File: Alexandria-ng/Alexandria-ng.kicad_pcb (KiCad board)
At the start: 4 copper layers, 87 parts, among them J1 Eth0, J10 PoE3, J11 PoE4, J12 FFC, J13 +3.3V, J14 I²C, J2 Eth1, J3 Eth2, J4 Eth3, J5 Eth4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

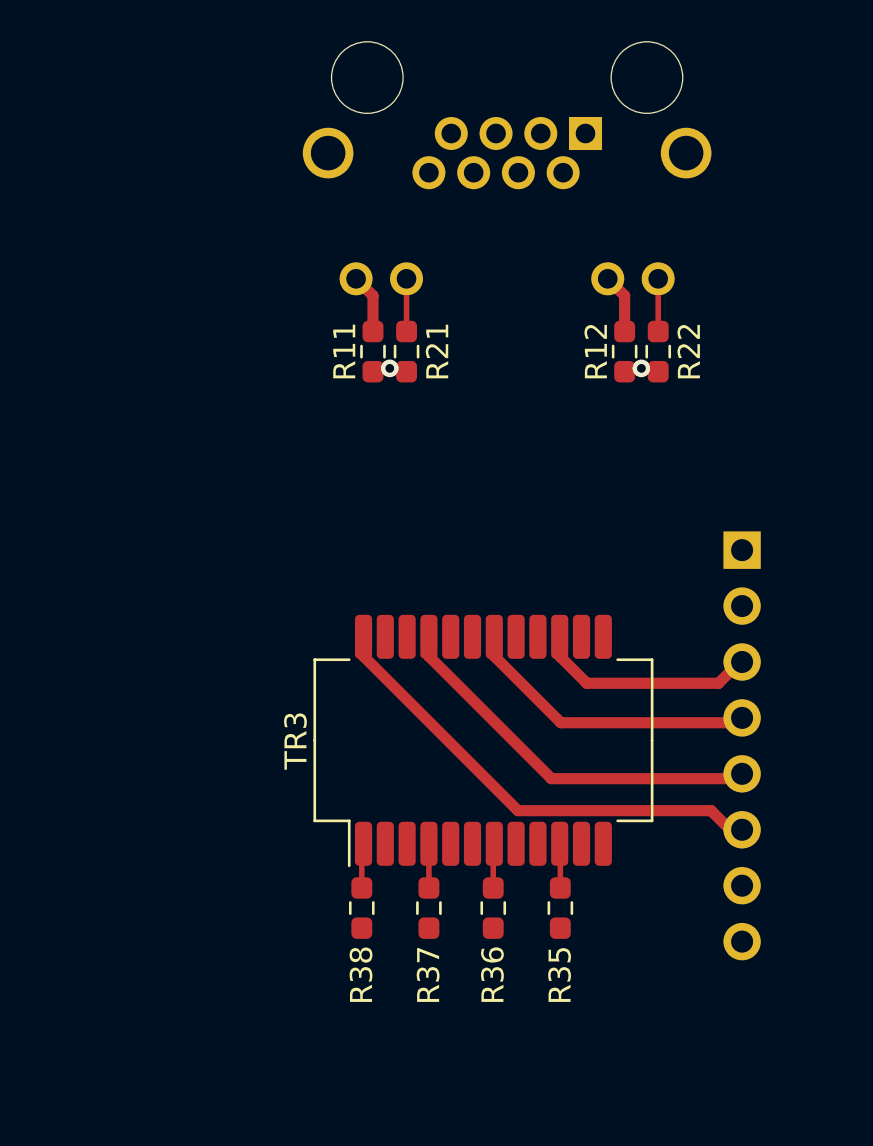
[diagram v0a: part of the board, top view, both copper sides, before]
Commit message: Re-doing Ethernet magnetics area
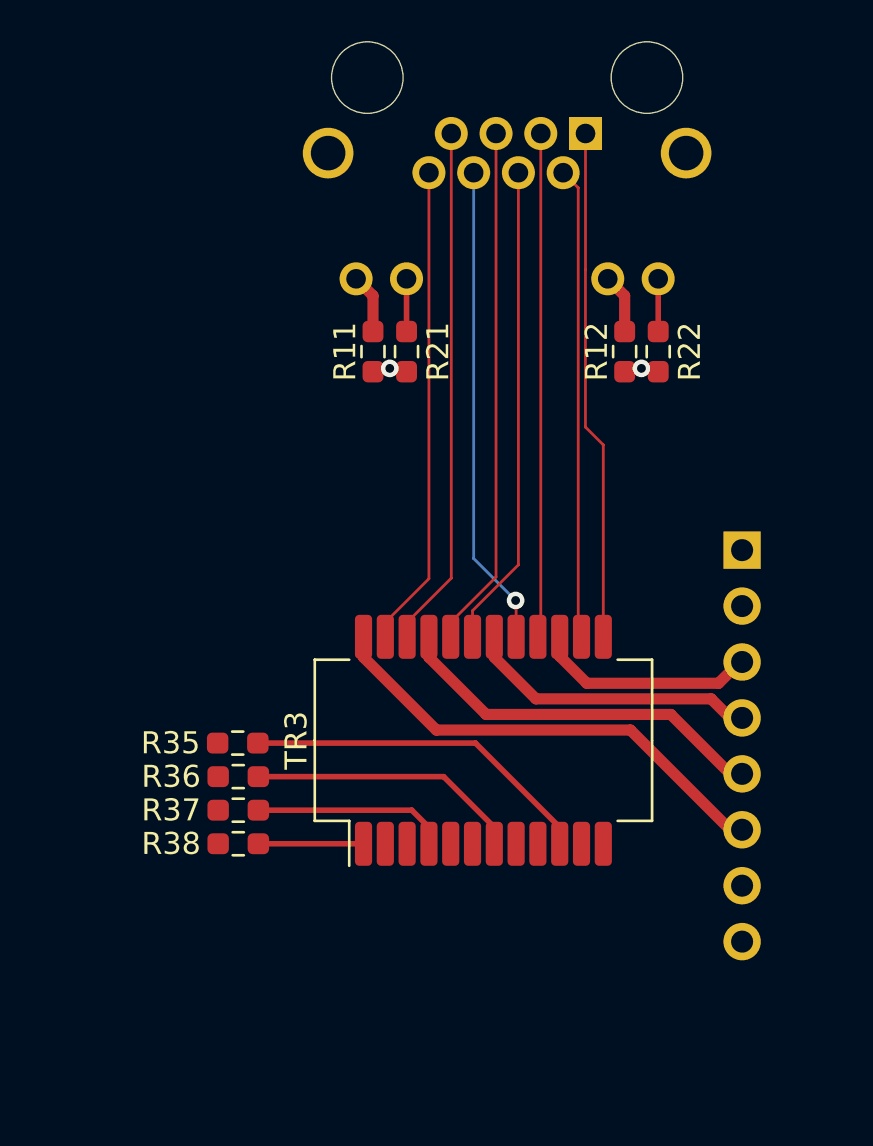
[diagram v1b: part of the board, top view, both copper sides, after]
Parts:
- moved R35 16.5 mm to (136.1, 60.7), turned to 180 degrees
- moved R36 13.0 mm to (136.1, 62.2), turned to 180 degrees
- moved R37 9.73 mm to (136.1, 63.8), turned to 180 degrees
- moved R38 6.33 mm to (136.1, 65.3), turned to 180 degrees
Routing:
- net P2CN: track 0.00 -> 23.7 mm
- net P2DP: track 0.00 -> 23.7 mm
- net P2AP: track 0.00 -> 23.2 mm
- net P2BP: track 0.00 -> 22.9 mm
- net P2CP: track 0.00 -> 21.9 mm
- net P2DN: track 0.00 -> 21.9 mm
- net P2BN: track 0.00 -> 21.9 mm, vias 0 -> 1
- net P2AN: track 0.00 -> 21.4 mm
- net E2AC: track 2.02 -> 16.1 mm
- net E2BC: track 2.03 -> 12.5 mm
- net E2CC: track 2.01 -> 8.82 mm
- net E2DC: track 2.04 -> 4.89 mm

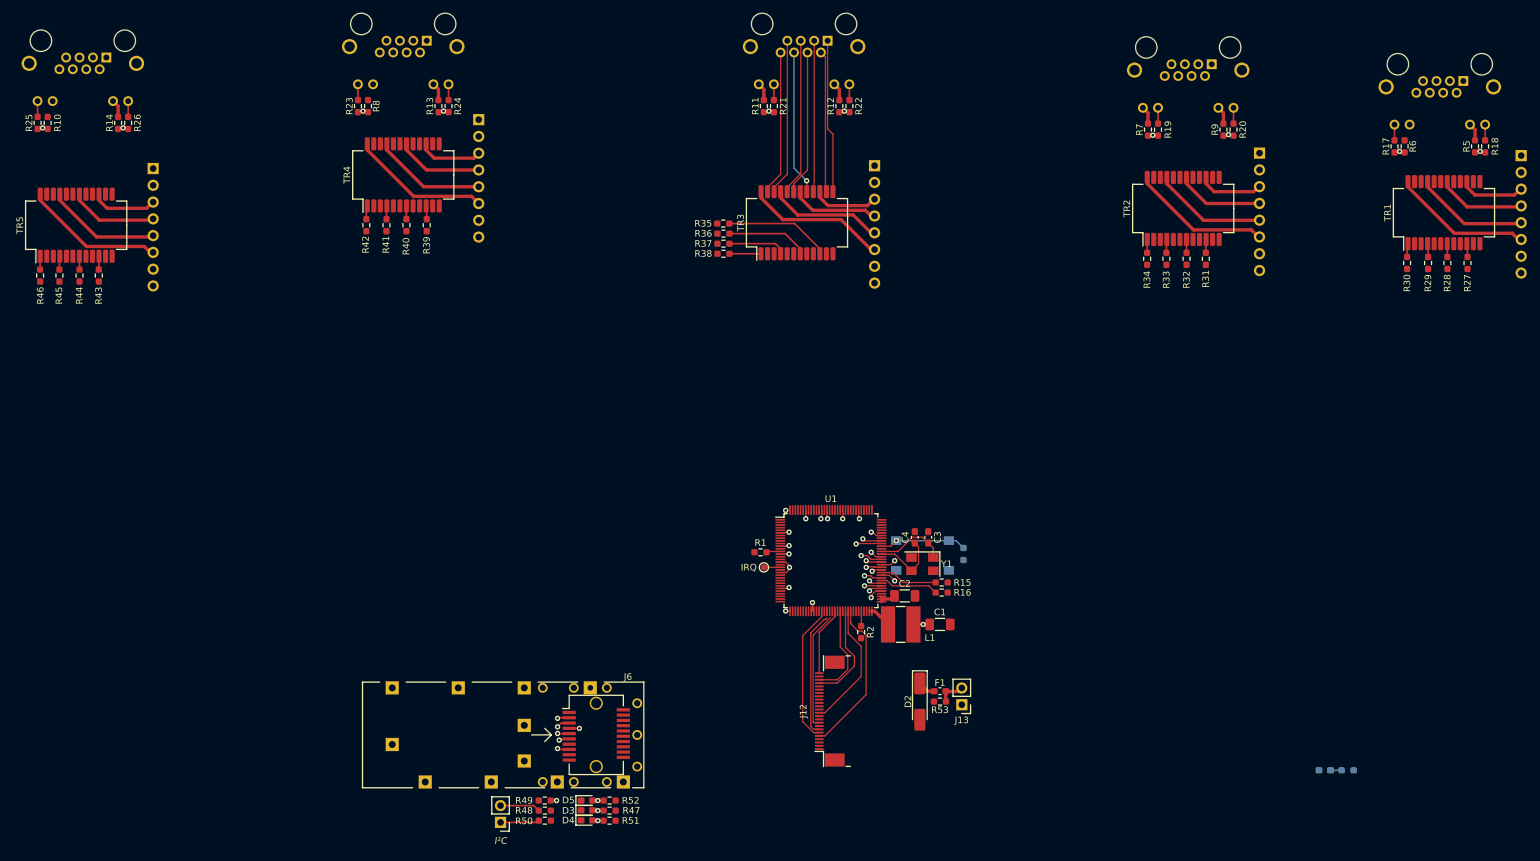
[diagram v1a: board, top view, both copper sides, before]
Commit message: Fixing some DRC errors
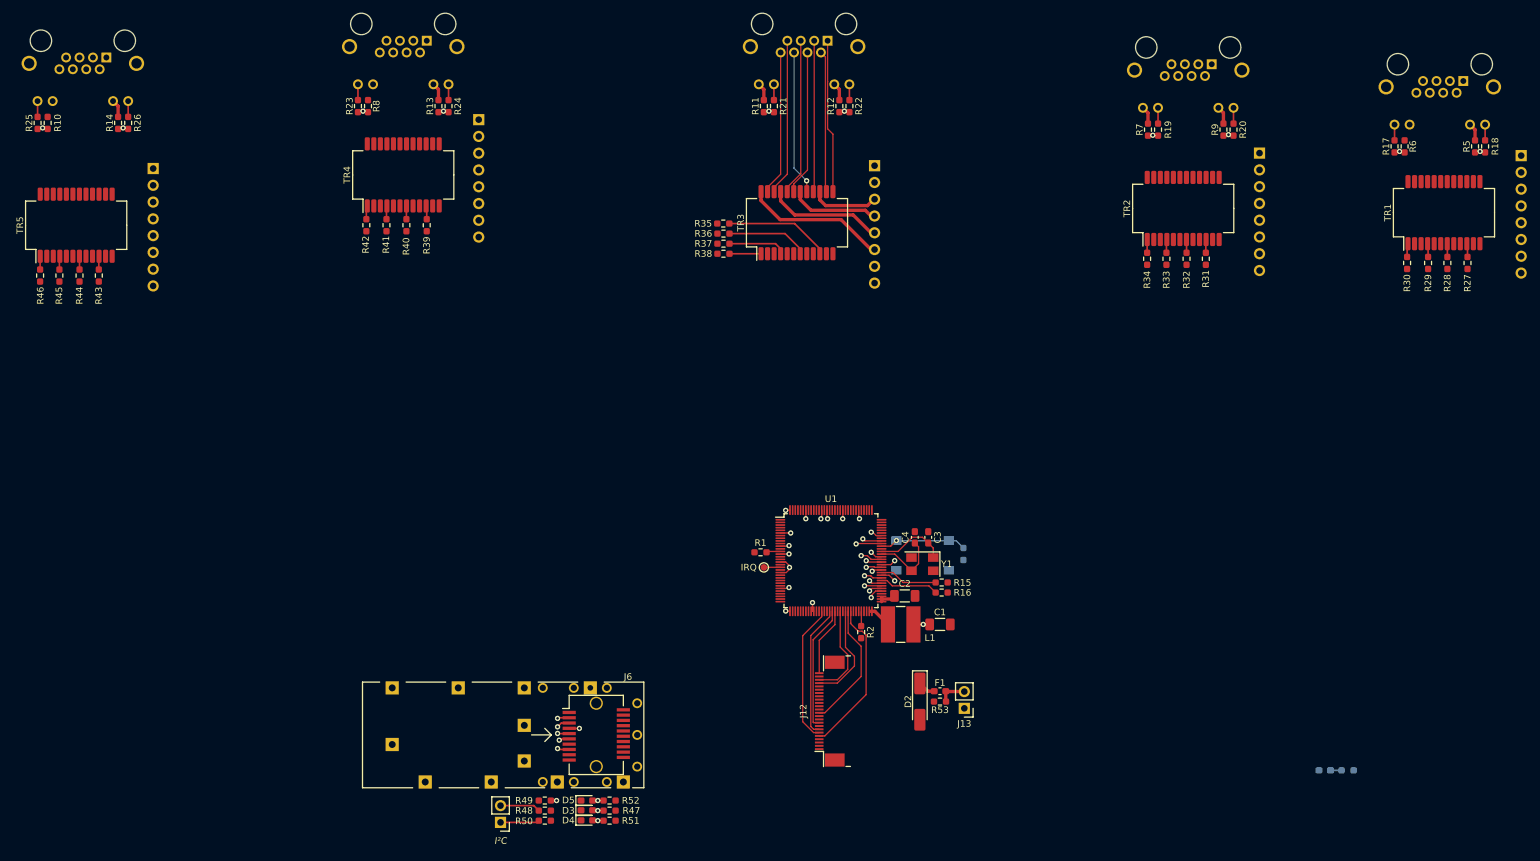
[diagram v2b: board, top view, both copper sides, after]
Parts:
- moved J13 0.66 mm to (172.6, 134.1)
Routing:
- net P4DC: track 21.2 -> 0.00 mm
- net P1DC: track 21.2 -> 0.00 mm
- net P3DC: track 21.2 -> 0.00 mm
- net P0DC: track 21.2 -> 0.00 mm
- net P0CC: track 17.1 -> 0.00 mm
- net P4CC: track 17.1 -> 0.00 mm
- net P3CC: track 17.1 -> 0.00 mm
- net P1CC: track 17.1 -> 0.00 mm
- net P0BC: track 13.1 -> 0.00 mm
- net P4BC: track 13.1 -> 0.00 mm
- net P3BC: track 13.1 -> 0.00 mm
- net P1BC: track 13.1 -> 0.00 mm
- net P1AC: track 9.71 -> 0.00 mm
- net P4AC: track 9.71 -> 0.00 mm
- net P0AC: track 9.71 -> 0.00 mm
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
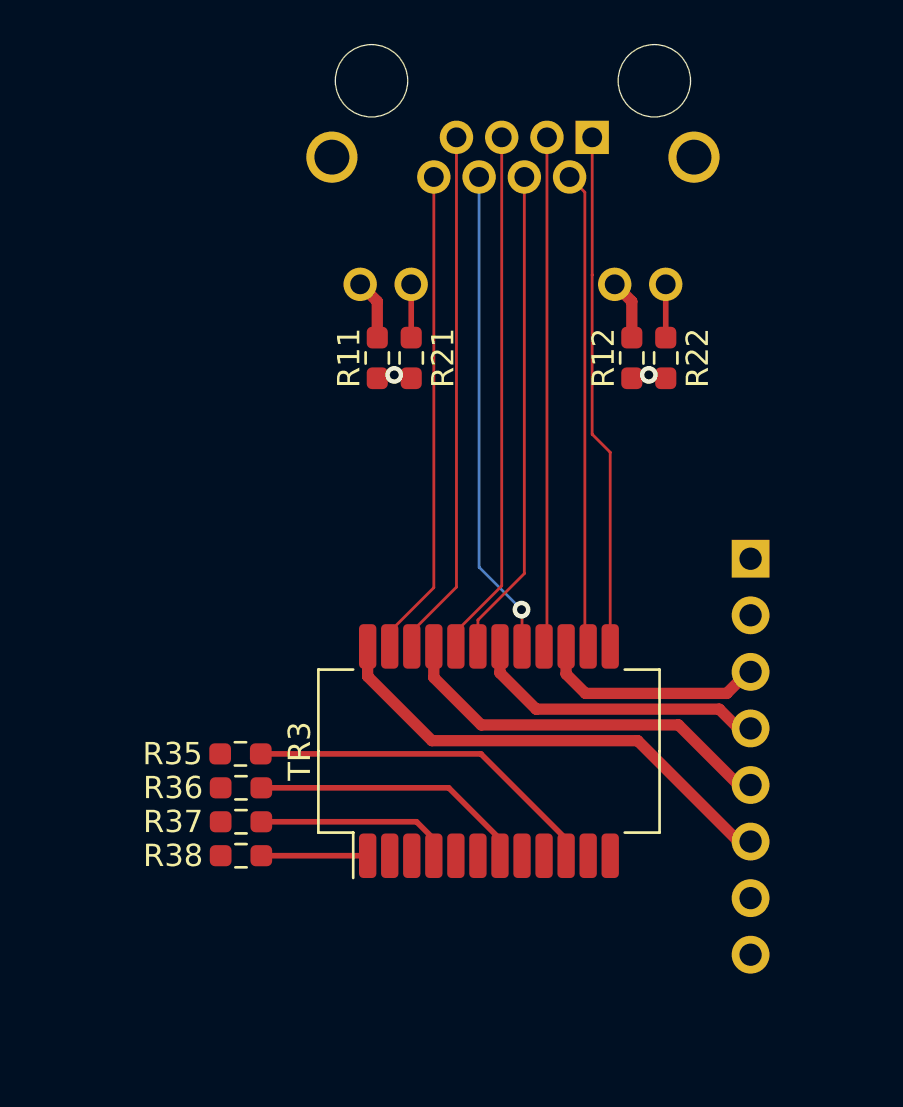
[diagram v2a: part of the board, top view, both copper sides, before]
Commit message: Tuning Ethernet MDI diff pairs at the RJ45 jack
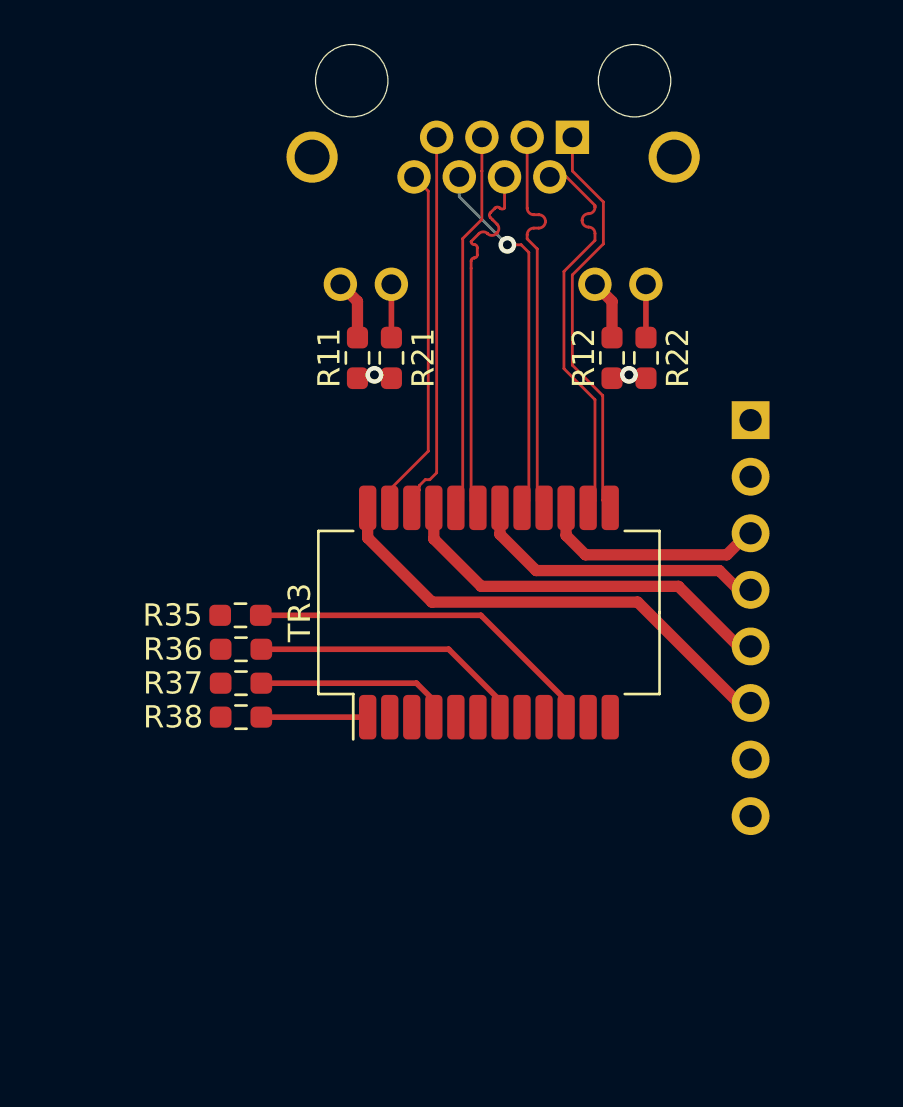
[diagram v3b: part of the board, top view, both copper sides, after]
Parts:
- moved R35 6.22 mm to (136.1, 54.5)
- moved R38 6.22 mm to (136.1, 59.1)
- moved J9 6.22 mm to (159.0, 45.7)
- moved R36 6.22 mm to (136.1, 56.0)
- moved R37 6.22 mm to (136.1, 57.5)
- moved TR3 6.22 mm to (147.3, 54.4)
- moved J3 0.89 mm to (151.0, 33.0)
- moved R11 0.89 mm to (141.4, 42.9)
- moved R21 0.89 mm to (142.9, 42.9)
- moved R12 0.89 mm to (152.8, 42.9)
- moved R22 0.89 mm to (154.3, 42.9)
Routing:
- net P2CN: track 23.7 -> 17.1 mm
- net P2DP: track 23.7 -> 17.2 mm
- net P2DN: track 21.9 -> 15.8 mm
- net P2BN: track 21.9 -> 16.6 mm
- net P2CP: track 21.9 -> 17.0 mm
- net P2BP: track 22.9 -> 18.0 mm
- net P2AP: track 23.2 -> 18.5 mm
- net P2AN: track 21.4 -> 18.0 mm
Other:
- board text added: "5 mil traces with 10 mil spacing and 15 mils from ground comes out at 102 Ω"
- board text added: "5.9 mil traces with 15 mil ground separation comes out to 50.86 Ω SE With 10 mil spacing, it gives 94.8 Ω differential"
- board text added: "Worst intra-pair skew: 415.9 µm (A pair) Allowed in total: 50 mil (1270 µm) Worst inter-pair skew: 2635.5 µm (DN-AP) Allowed in total: 600 mil (15240 µm) Source: https://ww1.microchip.com/downloads/en/Appnotes/00002054A.pdf"

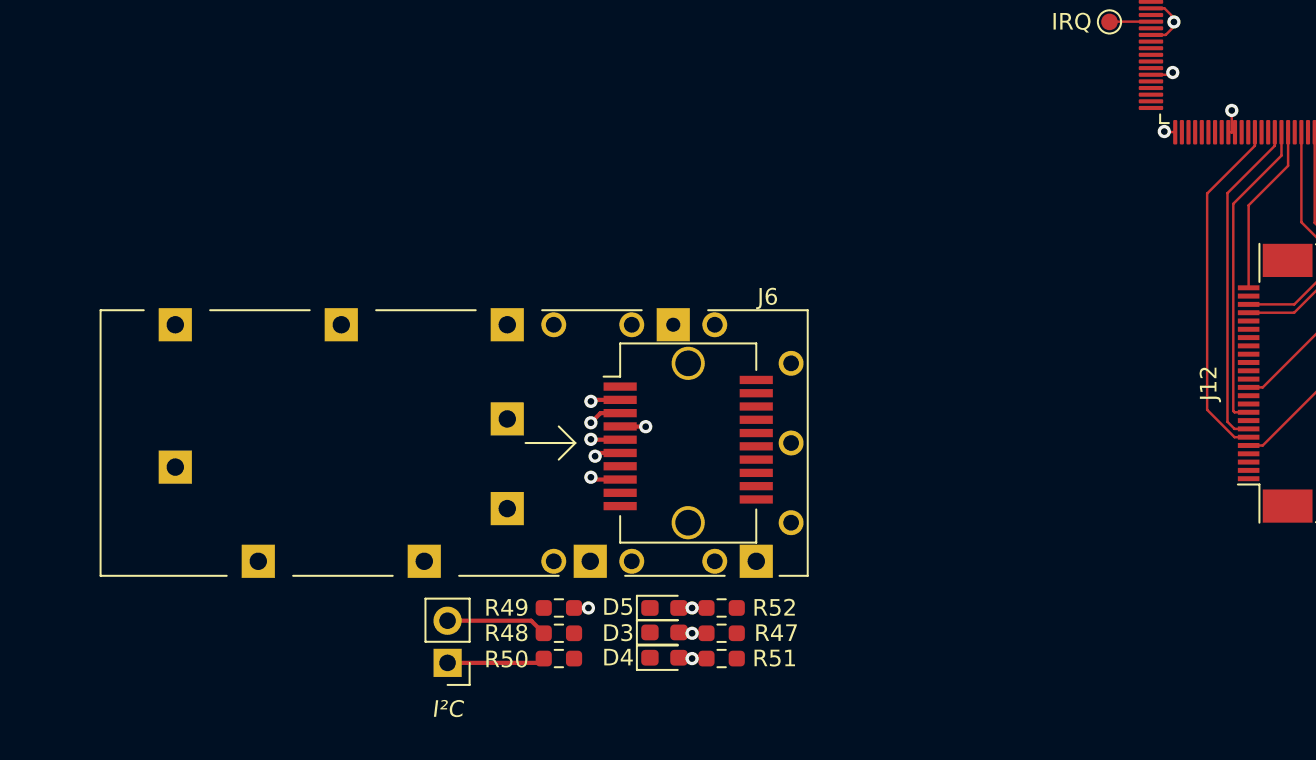
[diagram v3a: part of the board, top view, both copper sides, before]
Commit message: Routing SGMII to the SFP cage
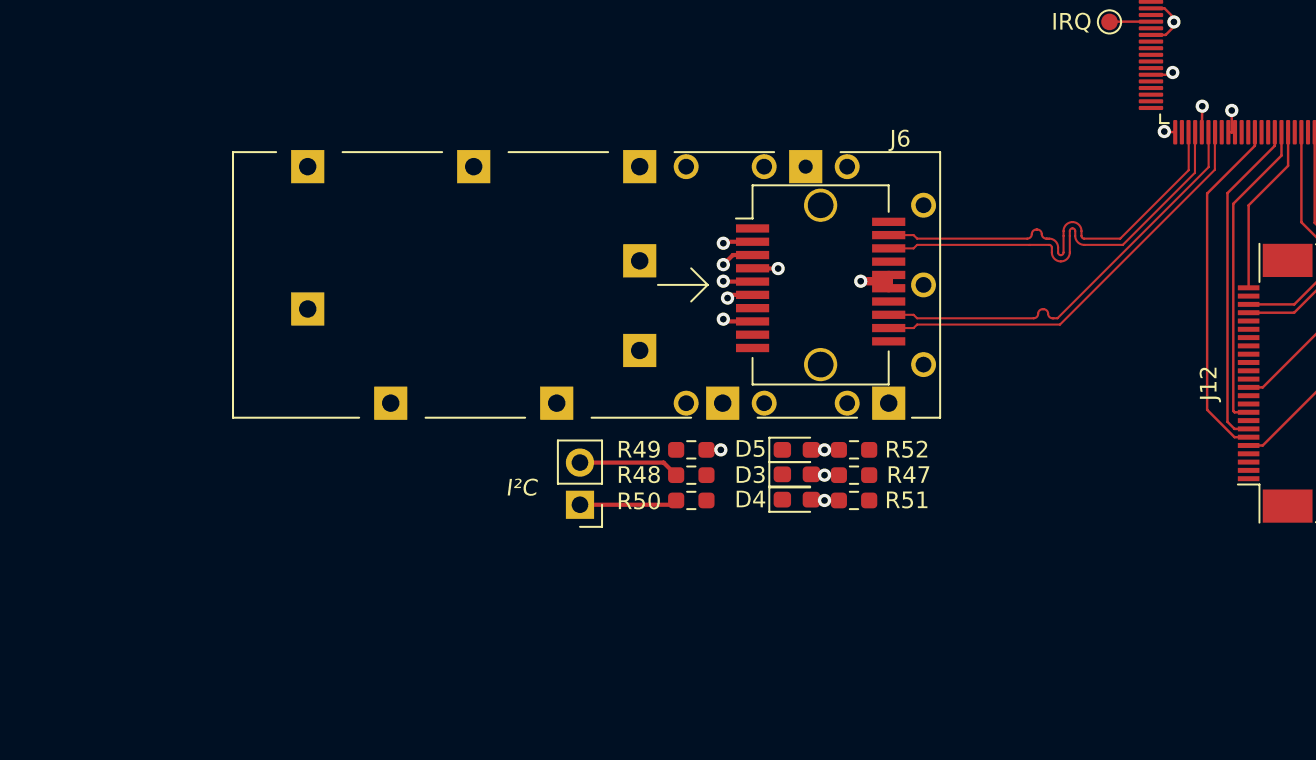
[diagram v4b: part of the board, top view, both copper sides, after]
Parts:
- moved J14 12.4 mm to (110.3, 141.9)
- moved R47 12.4 mm to (126.8, 140.1)
- moved R51 12.4 mm to (126.8, 141.6)
- moved R52 12.4 mm to (126.8, 138.6)
- moved D3 12.4 mm to (123.4, 140.0)
- moved D4 12.4 mm to (123.4, 141.6)
- moved D5 12.4 mm to (123.4, 138.6)
- moved J6 12.4 mm to (131.0, 128.6)
- moved R48 12.4 mm to (117.0, 140.1)
- moved R49 12.4 mm to (117.0, 138.6)
- moved R50 12.4 mm to (117.0, 141.6)
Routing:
- net HS_IN: track 0.00 -> 25.9 mm
- net HS_IP: track 0.00 -> 25.8 mm
- net HS_OP: track 0.00 -> 25.8 mm
- net HS_ON: track 0.00 -> 25.7 mm
- net +3.3V: track 39.2 -> 41.8 mm, vias 9 -> 10
- net +1V1: track 13.5 -> 15.1 mm, vias 8 -> 9
